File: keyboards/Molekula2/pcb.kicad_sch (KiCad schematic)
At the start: 93 parts, among them J1 N!N, J10 Conn_01x12_Socket, J11 Conn_01x12_Socket, J12 Conn_01x02_Socket, J2 C479750, J3 C479750, J4 C479750, J5 C479750, J6 Display_nice-view, J7 Conn_01x02_Socket, J8 C262499, J9 C262499, SW1 Switch, SW10 Switch, SW11 Switch, SW12 Switch, SW13 Switch, SW14 Switch, SW15 Switch, SW16 Switch, SW17 Switch, SW18 Switch, SW19 Switch, SW2 Switch, SW20 Switch, SW21 Switch, SW22 Switch, SW23 Switch, SW24 Switch, SW25 Switch, SW26 Switch, SW27 Switch, SW28 Switch, SW29 Switch, SW3 Switch, SW30 Switch, SW31 Switch, SW32 Switch, SW33 Switch, SW34 Switch, SW35 Switch, SW36 Switch, SW37 SW_Push, SW38 RotaryEncoder_Switch, SW4 Switch, SW5 Switch, SW6 Switch, SW7 Switch, SW8 Switch, SW9 Switch

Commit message: feat: add 2 more keys to the upper row and updated bom
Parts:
- added D37, D38: C81598, zzkeeb:Diode_1N4148-SOD123, symbol zzkeeb:Diode
- added SW39, SW40: Switch, zzkeeb:Switch_MXKSChoc-miny-hotswap-chocv2-3d, symbol zzkeeb:Switch
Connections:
- net col0: now also SW39.2
- net col9: now also SW40.2
- net row3: now also D37.1 (K)
- net row7: now also D38.1 (K)
- new net: D37.2 (A), SW39.1
- new net: D38.2 (A), SW40.1

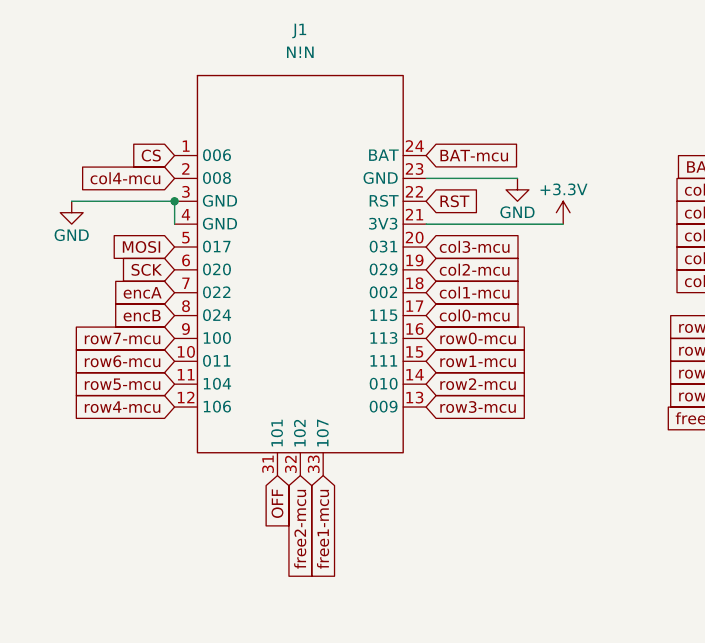
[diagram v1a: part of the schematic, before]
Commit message: feat: change MCU to RP2040
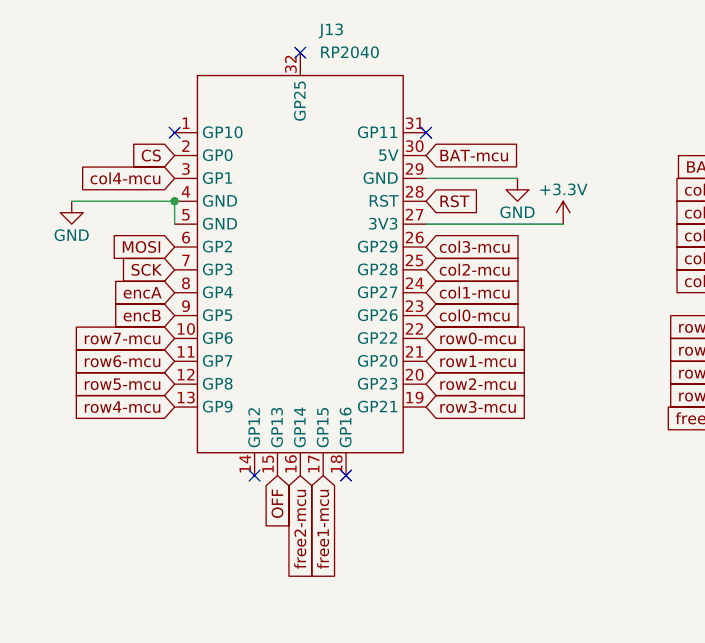
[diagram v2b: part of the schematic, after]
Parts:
- removed J1: N!N, zzkeeb:MCU_nice-nano, symbol zzkeeb:MCU_nice-nano
- added J13: RP2040, zzkeeb:MCU_rp2040-helios, symbol zzkeeb:MCU_rp2040-promicro-extend
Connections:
- net +3.3V: now also J13.27 (3V3)
- net BAT-mcu: now also J13.30 (5V)
- net CS: now also J13.2 (GP0)
- net GND: now also J13.29 (GND), J13.4 (GND), J13.5 (GND)
- net MOSI: now also J13.6 (GP2)
- net OFF: now also J13.15 (GP13)
- net RST: now also J13.28 (RST)
- net SCK: now also J13.7 (GP3)
- net col0-mcu: now also J13.23 (GP26)
- net col1-mcu: now also J13.24 (GP27)
- net col2-mcu: now also J13.25 (GP28)
- net col3-mcu: now also J13.26 (GP29)
- net col4-mcu: now also J13.3 (GP1)
- net encA: now also J13.8 (GP4)
- net encB: now also J13.9 (GP5)
- net free1-mcu: now also J13.17 (GP15)
- net free2-mcu: now also J13.16 (GP14)
- net row0-mcu: now also J13.22 (GP22)
- net row1-mcu: now also J13.21 (GP20)
- net row2-mcu: now also J13.20 (GP23)
- net row3-mcu: now also J13.19 (GP21)
- net row4-mcu: now also J13.13 (GP9)
- net row5-mcu: now also J13.12 (GP8)
- net row6-mcu: now also J13.11 (GP7)
- net row7-mcu: now also J13.10 (GP6)
- no-connect marks 2 -> 7
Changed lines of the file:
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@@
 	)
 	(junction
+		(at 45.72 38.1)
+		(diameter 0)
+		(color 0 0 0 0)
+	)
+	(junction
 		(at 57.15 142.24)
 		(diameter 0)
@@
 	)
 	(junction
-		(at 45.72 38.1)
-		(diameter 0)
-		(color 0 0 0 0)
-	)
-	(junction
 		(at 90.17 113.03)
 		(diameter 0)
@@
 	)
 	(no_connect
+		(at 45.72 30.48)
+	)
+	(no_connect
+		(at 73.66 30.48)
+	)
+	(no_connect
 		(at 105.41 238.76)
 	)
 	(no_connect
+		(at 59.69 21.59)
+	)
+	(no_connect
+		(at 54.61 68.58)
+	)
+	(no_connect
+		(at 64.77 68.58)
+	)
+	(no_connect
 		(at 46.99 266.7)
 	)
@@
 	)
 	(symbol
-		(lib_id "zzkeeb:MCU_nice-nano")
-		(at 59.69 45.72 0)
-		(unit 1)
-		(exclude_from_sim no)
-		(in_bom yes)
-		(on_board yes)
-		(dnp no)
-		(fields_autoplaced yes)
-		(property "Reference" "J1"
-			(at 59.69 19.05 0)
-			(effects
-				(font
-					(size 1.27 1.27)
-				)
-			)
-		)
-		(property "Value" "N!N"
-			(at 59.69 21.59 0)
-			(effects
-				(font
-					(size 1.27 1.27)
-				)
-			)
-		)
-		(property "Footprint" "zzkeeb:MCU_nice-nano"
-			(at 59.69 48.26 0)
-			(effects
-				(font
-					(size 1.27 1.27)
-				)
-				(hide yes)
-			)
-		)
-		(property "Datasheet" ""
-			(at 59.69 48.26 0)
-			(effects
-				(font
-					(size 1.27 1.27)
-				)
-				(hide yes)
-			)
-		)
-		(property "Description" ""
-			(at 59.69 45.72 0)
-			(effects
-				(font
-					(size 1.27 1.27)
-				)
-				(hide yes)
-			)
-		)
-		(pin "1"
-		)
-		(pin "10"
-		)
-		(pin "11"
-		)
-		(pin "12"
-		)
-		(pin "13"
-		)
-		(pin "14"
-		)
-		(pin "15"
-		)
-		(pin "16"
-		)
-		(pin "17"
-		)
-		(pin "18"
-		)
-		(pin "19"
-		)
-		(pin "2"
-		)
-		(pin "20"
-		)
-		(pin "21"
-		)
-		(pin "22"
-		)
-		(pin "23"
-		)
-		(pin "24"
-		)
-		(pin "3"
-		)
-		(pin "31"
-		)
-		(pin "32"
-		)
-		(pin "33"
-		)
-		(pin "4"
-		)
-		(pin "5"
-		)
-		(pin "6"
-		)
-		(pin "7"
-		)
-		(pin "8"
-		)
-		(pin "9"
-		)
-		(instances
-			(project "pcb"
-				(path "/2f68eba7-4e8a-4af0-a221-669d7c557d47"
-					(reference "J1")
-					(unit 1)
-				)
-			)
-		)
-	)
-	(symbol
 		(lib_id "zzkeeb:Switch")
 		(at 64.77 153.67 0)
@@
 					(unit 1)
 				)
+			)
+		)
+	)
+	(symbol
+		(lib_id "zzkeeb:MCU_rp2040-promicro-extend")
+		(at 59.69 45.72 0)
+		(unit 1)
+		(exclude_from_sim no)
+		(in_bom yes)
+		(on_board yes)
+		(dnp no)
+		(fields_autoplaced yes)
+		(property "Reference" "J13"
+			(at 61.8333 19.05 0)
+			(effects
+				(font
+					(size 1.27 1.27)
+				)
+				(justify left)
+			)
+		)
+		(property "Value" "RP2040"
+			(at 61.8333 21.59 0)
+			(effects
+				(font
+					(size 1.27 1.27)
+				)
+				(justify left)
+			)
+		)
+		(property "Footprint" "zzkeeb:MCU_rp2040-helios"
+			(at 59.69 48.26 0)
+			(effects
+				(font
+					(size 1.27 1.27)
+				)
+				(hide yes)
+			)
+		)
+		(property "Datasheet" ""
+			(at 59.69 48.26 0)
+			(effects
+				(font
+					(size 1.27 1.27)
+				)
+				(hide yes)
+			)
+		)
+		(property "Description" ""
+			(at 59.69 45.72 0)
+			(effects
+				(font
+					(size 1.27 1.27)
+				)
+				(hide yes)
+			)
+		)
+		(pin "14"
+		)
+		(pin "5"
+		)
+		(pin "12"
+		)
+		(pin "16"
+		)
+		(pin "1"
+		)
+		(pin "2"
+		)
+		(pin "3"
+		)
+		(pin "6"
+		)
+		(pin "9"
+		)
+		(pin "32"
+		)
+		(pin "4"
+		)
+		(pin "8"
+		)
+		(pin "7"
+		)
+		(pin "10"
+		)
+		(pin "11"
+		)
+		(pin "13"
+		)
+		(pin "17"
+		)
+		(pin "18"
+		)
+		(pin "31"
+		)
+		(pin "15"
+		)
+		(pin "30"
+		)
+		(pin "29"
+		)
+		(pin "28"
+		)
+		(pin "27"
+		)
+		(pin "26"
+		)
+		(pin "25"
+		)
+		(pin "24"
+		)
+		(pin "23"
+		)
+		(pin "22"
+		)
+		(pin "19"
+		)
+		(pin "21"
+		)
+		(pin "20"
+		)
+		(instances
+			(project ""
+				(path "/2f68eba7-4e8a-4af0-a221-669d7c557d47"
+					(reference "J13")
+					(unit 1)
+				)
